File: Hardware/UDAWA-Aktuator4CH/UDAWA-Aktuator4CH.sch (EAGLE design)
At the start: 20 parts

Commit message: PCB Print Ready
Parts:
- added RELAY_PWR: (no value), con-wago-500:W237-102
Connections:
- net 5V: now also RELAY_PWR-2.KL
- net GND: now also RELAY_PWR-1.KL
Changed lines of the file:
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@@
 </class>
 </classes>
-<groups>
-<schematic_group name="RELAY_CONTROL"/>
-</groups>
 <parts>
 <part name="U$1" library="ESP32-DEVKITV1" deviceset="ESP32DEVKITV1" device=""/>
@@
 <part name="CH4" library="con-wago-500" deviceset="W237-102" device="" package3d_urn="urn:adsk.eagle:package:10688/1"/>
 <part name="MAIN_IN" library="con-wago-500" deviceset="W237-102" device="" package3d_urn="urn:adsk.eagle:package:10688/1"/>
+<part name="RELAY_PWR" library="con-wago-500" deviceset="W237-102" device="" package3d_urn="urn:adsk.eagle:package:10688/1"/>
 </parts>
 <sheets>
@@
 <attribute name="NAME" x="-43.18" y="21.209" size="1.778" layer="95" rot="R180"/>
 </instance>
-<instance part="RELAY1" gate="-1" x="86.36" y="-15.24" smashed="yes" grouprefs="RELAY_CONTROL">
+<instance part="RELAY1" gate="-1" x="86.36" y="-15.24" smashed="yes">
 <attribute name="NAME" x="86.36" y="-14.351" size="1.778" layer="95" rot="R180"/>
 </instance>
-<instance part="RELAY1" gate="-2" x="86.36" y="-20.32" smashed="yes" grouprefs="RELAY_CONTROL">
+<instance part="RELAY1" gate="-2" x="86.36" y="-20.32" smashed="yes">
 <attribute name="VALUE" x="83.82" y="-24.003" size="1.778" layer="96"/>
 <attribute name="NAME" x="86.36" y="-19.431" size="1.778" layer="95" rot="R180"/>
 </instance>
-<instance part="RELAY2" gate="-1" x="86.36" y="-5.08" smashed="yes" grouprefs="RELAY_CONTROL">
+<instance part="RELAY2" gate="-1" x="86.36" y="-5.08" smashed="yes">
 <attribute name="NAME" x="86.36" y="-4.191" size="1.778" layer="95" rot="R180"/>
 </instance>
-<instance part="RELAY2" gate="-2" x="86.36" y="-10.16" smashed="yes" grouprefs="RELAY_CONTROL">
+<instance part="RELAY2" gate="-2" x="86.36" y="-10.16" smashed="yes">
 <attribute name="VALUE" x="83.82" y="-13.843" size="1.778" layer="96"/>
 <attribute name="NAME" x="86.36" y="-9.271" size="1.778" layer="95" rot="R180"/>
@@
 <attribute name="VALUE" x="-13.97" y="-66.421" size="1.778" layer="96"/>
 </instance>
-<instance part="RELAY3" gate="-1" x="86.36" y="5.08" smashed="yes" grouprefs="RELAY_CONTROL">
+<instance part="RELAY3" gate="-1" x="86.36" y="5.08" smashed="yes">
 <attribute name="NAME" x="86.36" y="5.969" size="1.778" layer="95" rot="R180"/>
 </instance>
-<instance part="RELAY3" gate="-2" x="86.36" y="0" smashed="yes" grouprefs="RELAY_CONTROL">
+<instance part="RELAY3" gate="-2" x="86.36" y="0" smashed="yes">
 <attribute name="VALUE" x="83.82" y="-3.683" size="1.778" layer="96"/>
 <attribute name="NAME" x="86.36" y="0.889" size="1.778" layer="95" rot="R180"/>
 </instance>
-<instance part="RELAY4" gate="-1" x="86.36" y="15.24" smashed="yes" grouprefs="RELAY_CONTROL">
+<instance part="RELAY4" gate="-1" x="86.36" y="15.24" smashed="yes">
 <attribute name="NAME" x="86.36" y="16.129" size="1.778" layer="95" rot="R180"/>
 </instance>
-<instance part="RELAY4" gate="-2" x="86.36" y="10.16" smashed="yes" grouprefs="RELAY_CONTROL">
+<instance part="RELAY4" gate="-2" x="86.36" y="10.16" smashed="yes">
 <attribute name="VALUE" x="83.82" y="6.477" size="1.778" layer="96"/>
 <attribute name="NAME" x="86.36" y="11.049" size="1.778" layer="95" rot="R180"/>
@@
 <attribute name="VALUE" x="-55.88" y="-24.003" size="1.778" layer="96"/>
 <attribute name="NAME" x="-53.34" y="-19.431" size="1.778" layer="95" rot="R180"/>
+</instance>
+<instance part="RELAY_PWR" gate="-1" x="86.36" y="-27.94" smashed="yes">
+<attribute name="NAME" x="86.36" y="-27.051" size="1.778" layer="95" rot="R180"/>
+</instance>
+<instance part="RELAY_PWR" gate="-2" x="86.36" y="-33.02" smashed="yes">
+<attribute name="VALUE" x="83.82" y="-36.703" size="1.778" layer="96"/>
+<attribute name="NAME" x="86.36" y="-32.131" size="1.778" layer="95" rot="R180"/>
 </instance>
 </instances>
@@
 <segment>
 <pinref part="RELAY1" gate="-1" pin="KL"/>
-<wire x1="91.44" y1="-15.24" x2="93.98" y2="-15.24" width="0.1524" layer="91" grouprefs="RELAY_CONTROL"/>
-<label x="93.98" y="-15.24" size="1.27" layer="95" xref="yes" grouprefs="RELAY_CONTROL"/>
+<wire x1="91.44" y1="-15.24" x2="93.98" y2="-15.24" width="0.1524" layer="91"/>
+<label x="93.98" y="-15.24" size="1.27" layer="95" xref="yes"/>
 </segment>
 <segment>
 <pinref part="RELAY2" gate="-1" pin="KL"/>
-<wire x1="91.44" y1="-5.08" x2="93.98" y2="-5.08" width="0.1524" layer="91" grouprefs="RELAY_CONTROL"/>
-<label x="93.98" y="-5.08" size="1.27" layer="95" xref="yes" grouprefs="RELAY_CONTROL"/>
+<wire x1="91.44" y1="-5.08" x2="93.98" y2="-5.08" width="0.1524" layer="91"/>
+<label x="93.98" y="-5.08" size="1.27" layer="95" xref="yes"/>
 </segment>
 <segment>
 <pinref part="RELAY3" gate="-1" pin="KL"/>
-<wire x1="91.44" y1="5.08" x2="93.98" y2="5.08" width="0.1524" layer="91" grouprefs="RELAY_CONTROL"/>
-<label x="93.98" y="5.08" size="1.27" layer="95" xref="yes" grouprefs="RELAY_CONTROL"/>
+<wire x1="91.44" y1="5.08" x2="93.98" y2="5.08" width="0.1524" layer="91"/>
+<label x="93.98" y="5.08" size="1.27" layer="95" xref="yes"/>
 </segment>
 <segment>
 <pinref part="RELAY4" gate="-1" pin="KL"/>
-<wire x1="91.44" y1="15.24" x2="93.98" y2="15.24" width="0.1524" layer="91" grouprefs="RELAY_CONTROL"/>
-<label x="93.98" y="15.24" size="1.27" layer="95" xref="yes" grouprefs="RELAY_CONTROL"/>
+<wire x1="91.44" y1="15.24" x2="93.98" y2="15.24" width="0.1524" layer="91"/>
+<label x="93.98" y="15.24" size="1.27" layer="95" xref="yes"/>
+</segment>
+<segment>
+<pinref part="RELAY_PWR" gate="-1" pin="KL"/>
+<wire x1="91.44" y1="-27.94" x2="93.98" y2="-27.94" width="0.1524" layer="91"/>
+<label x="93.98" y="-27.94" size="1.778" layer="95" xref="yes"/>
 </segment>
 </net>
@@
 <label x="22.86" y="17.78" size="1.524" layer="95" rot="R90" xref="yes"/>
 </segment>
+<segment>
+<pinref part="RELAY_PWR" gate="-2" pin="KL"/>
+<wire x1="91.44" y1="-33.02" x2="93.98" y2="-33.02" width="0.1524" layer="91"/>
+<label x="93.98" y="-33.02" size="1.778" layer="95" xref="yes"/>
+</segment>
 </net>
 <net name="AC1" class="0">
@@
 <segment>
 <pinref part="RELAY4" gate="-2" pin="KL"/>
-<wire x1="91.44" y1="10.16" x2="93.98" y2="10.16" width="0.1524" layer="91" grouprefs="RELAY_CONTROL"/>
-<label x="93.98" y="10.16" size="1.27" layer="95" xref="yes" grouprefs="RELAY_CONTROL"/>
+<wire x1="91.44" y1="10.16" x2="93.98" y2="10.16" width="0.1524" layer="91"/>
+<label x="93.98" y="10.16" size="1.27" layer="95" xref="yes"/>
 </segment>
 </net>
@@
 <segment>
 <pinref part="RELAY3" gate="-2" pin="KL"/>
-<wire x1="91.44" y1="0" x2="93.98" y2="0" width="0.1524" layer="91" grouprefs="RELAY_CONTROL"/>
-<label x="93.98" y="0" size="1.27" layer="95" xref="yes" grouprefs="RELAY_CONTROL"/>
+<wire x1="91.44" y1="0" x2="93.98" y2="0" width="0.1524" layer="91"/>
+<label x="93.98" y="0" size="1.27" layer="95" xref="yes"/>
 </segment>
 </net>
@@
 <segment>
 <pinref part="RELAY2" gate="-2" pin="KL"/>
-<wire x1="91.44" y1="-10.16" x2="93.98" y2="-10.16" width="0.1524" layer="91" grouprefs="RELAY_CONTROL"/>
-<label x="93.98" y="-10.16" size="1.27" layer="95" xref="yes" grouprefs="RELAY_CONTROL"/>
+<wire x1="91.44" y1="-10.16" x2="93.98" y2="-10.16" width="0.1524" layer="91"/>
+<label x="93.98" y="-10.16" size="1.27" layer="95" xref="yes"/>
 </segment>
 </net>
@@
 <segment>
 <pinref part="RELAY1" gate="-2" pin="KL"/>
-<wire x1="91.44" y1="-20.32" x2="93.98" y2="-20.32" width="0.1524" layer="91" grouprefs="RELAY_CONTROL"/>
-<label x="93.98" y="-20.32" size="1.27" layer="95" xref="yes" grouprefs="RELAY_CONTROL"/>
+<wire x1="91.44" y1="-20.32" x2="93.98" y2="-20.32" width="0.1524" layer="91"/>
+<label x="93.98" y="-20.32" size="1.27" layer="95" xref="yes"/>
 </segment>
 </net>
@@
 packages will not be understood (or retained) with this version.
 </note>
-<note version="9.5" severity="warning">
-Since Version 9.5, EAGLE supports persistent groups with
-schematics, and board files. Those persistent groups
-will not be understood (or retained) with this version.
-</note>
 </compatibility>

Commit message: Revisi terminal catu daya. Solar panel support.
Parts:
- added MCU_PWR_IN, PSU_5V: (no value), con-wago-500:W237-102
- renumbered MAIN_IN to LOAD_IN
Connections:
- net VCC renamed 3V3
- removed net GND2: U$1.GND@2
- new net VIN: MCU_PWR_IN-2.KL, U$1.VIN
- net 5V: now also PSU_5V-2.KL; no longer U$1.VIN
- net GND: now also MCU_PWR_IN-1.KL, PSU_5V-1.KL, U$1.GND@2

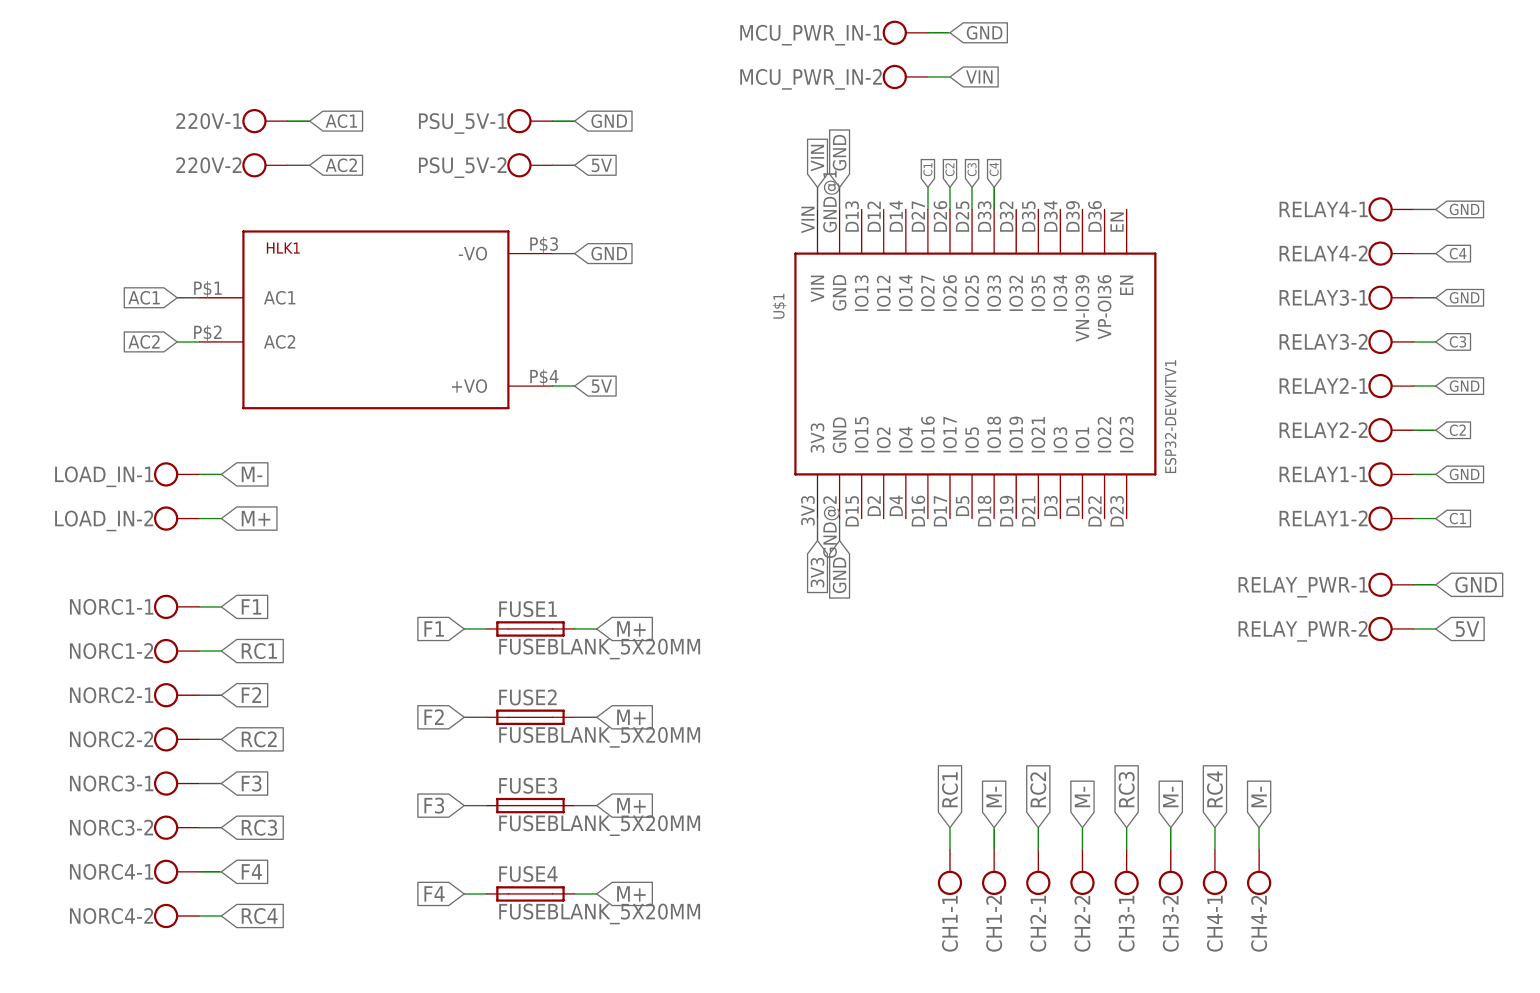
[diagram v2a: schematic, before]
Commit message: revisi fuse holder ke SH22,5A (Version 1)
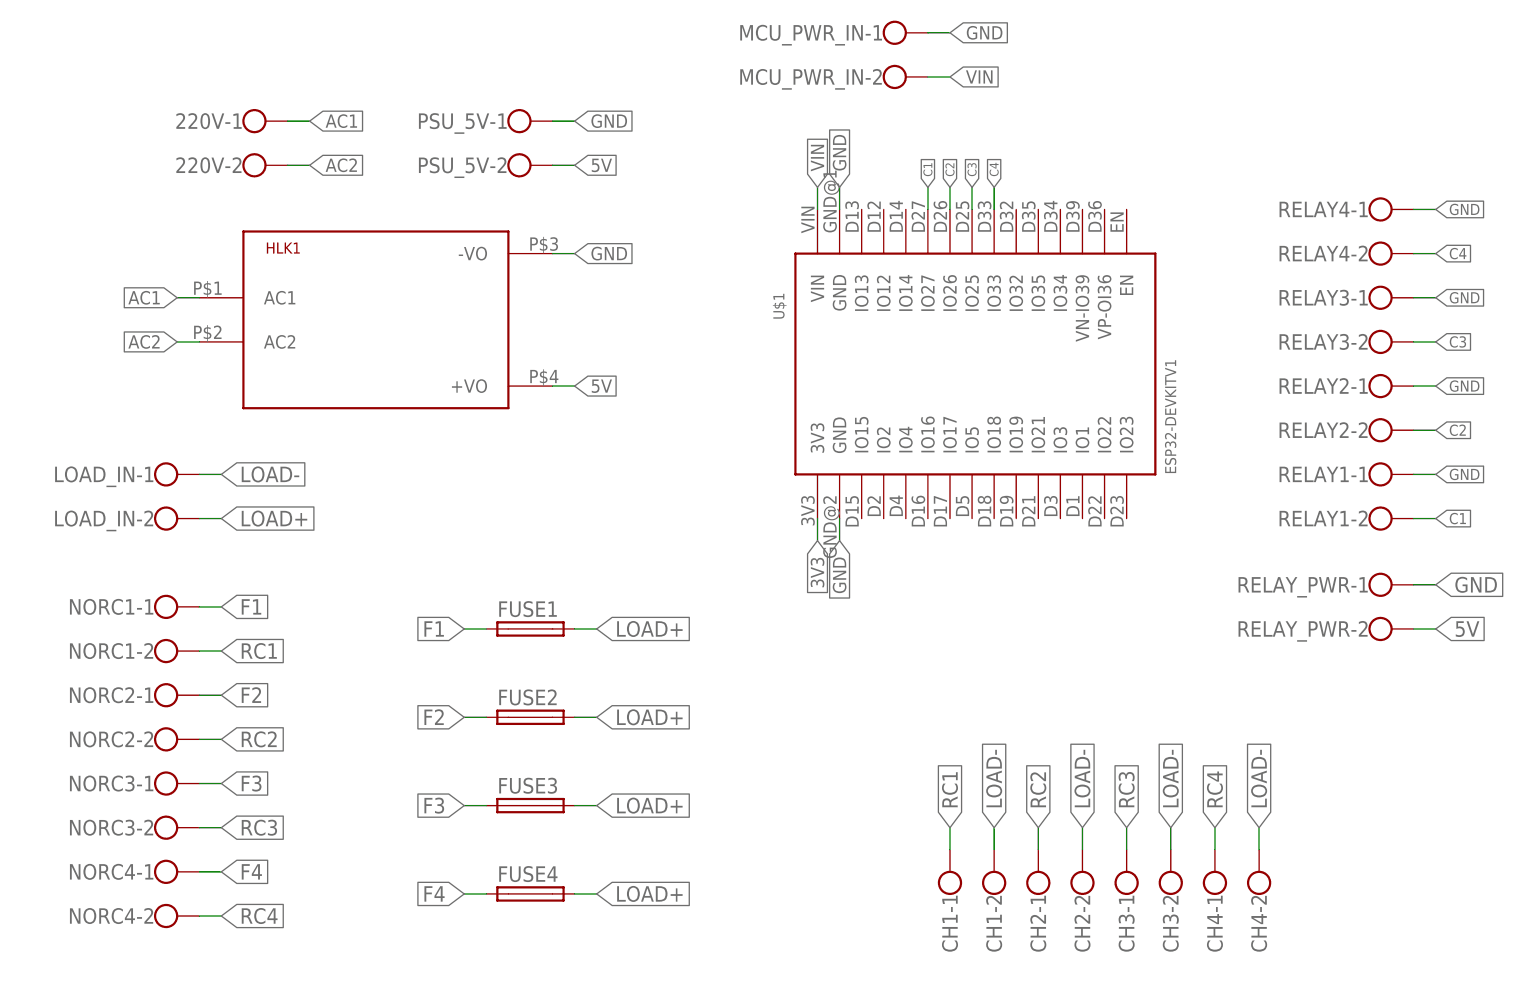
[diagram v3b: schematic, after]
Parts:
- FUSE1, FUSE2, FUSE3, FUSE4: value FUSEBLANK_5X20MM -> (none); device fuse:FUSEBLANK_5X20MM -> fuse:SH22,5A
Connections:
- net M+ renamed LOAD+
- net M- renamed LOAD-
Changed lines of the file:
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@@
 <part name="RELAY1" library="con-wago-500" deviceset="W237-102" device="" package3d_urn="urn:adsk.eagle:package:10688/1"/>
 <part name="RELAY2" library="con-wago-500" deviceset="W237-102" device="" package3d_urn="urn:adsk.eagle:package:10688/1"/>
-<part name="FUSE1" library="fuse" deviceset="FUSE" device="BLANK_5X20MM" package3d_urn="urn:adsk.eagle:package:14079/1"/>
-<part name="FUSE2" library="fuse" deviceset="FUSE" device="BLANK_5X20MM" package3d_urn="urn:adsk.eagle:package:14079/1"/>
-<part name="FUSE3" library="fuse" deviceset="FUSE" device="BLANK_5X20MM" package3d_urn="urn:adsk.eagle:package:14079/1"/>
-<part name="FUSE4" library="fuse" deviceset="FUSE" device="BLANK_5X20MM" package3d_urn="urn:adsk.eagle:package:14079/1"/>
+<part name="FUSE1" library="fuse" deviceset="SH22,5A" device="" package3d_urn="urn:adsk.eagle:package:14070/1"/>
+<part name="FUSE2" library="fuse" deviceset="SH22,5A" device="" package3d_urn="urn:adsk.eagle:package:14070/1"/>
+<part name="FUSE3" library="fuse" deviceset="SH22,5A" device="" package3d_urn="urn:adsk.eagle:package:14070/1"/>
+<part name="FUSE4" library="fuse" deviceset="SH22,5A" device="" package3d_urn="urn:adsk.eagle:package:14070/1"/>
 <part name="RELAY3" library="con-wago-500" deviceset="W237-102" device="" package3d_urn="urn:adsk.eagle:package:10688/1"/>
 <part name="RELAY4" library="con-wago-500" deviceset="W237-102" device="" package3d_urn="urn:adsk.eagle:package:10688/1"/>
@@
 <attribute name="NAME" x="86.36" y="-9.271" size="1.778" layer="95" rot="R180"/>
 </instance>
-<instance part="FUSE1" gate="G$1" x="-10.16" y="-33.02" smashed="yes">
+<instance part="FUSE1" gate="1" x="-10.16" y="-33.02" smashed="yes">
 <attribute name="NAME" x="-13.97" y="-31.623" size="1.778" layer="95"/>
 <attribute name="VALUE" x="-13.97" y="-35.941" size="1.778" layer="96"/>
 </instance>
-<instance part="FUSE2" gate="G$1" x="-10.16" y="-43.18" smashed="yes">
+<instance part="FUSE2" gate="1" x="-10.16" y="-43.18" smashed="yes">
 <attribute name="NAME" x="-13.97" y="-41.783" size="1.778" layer="95"/>
 <attribute name="VALUE" x="-13.97" y="-46.101" size="1.778" layer="96"/>
 </instance>
-<instance part="FUSE3" gate="G$1" x="-10.16" y="-53.34" smashed="yes">
+<instance part="FUSE3" gate="1" x="-10.16" y="-53.34" smashed="yes">
 <attribute name="NAME" x="-13.97" y="-51.943" size="1.778" layer="95"/>
 <attribute name="VALUE" x="-13.97" y="-56.261" size="1.778" layer="96"/>
 </instance>
-<instance part="FUSE4" gate="G$1" x="-10.16" y="-63.5" smashed="yes">
+<instance part="FUSE4" gate="1" x="-10.16" y="-63.5" smashed="yes">
 <attribute name="NAME" x="-13.97" y="-62.103" size="1.778" layer="95"/>
 <attribute name="VALUE" x="-13.97" y="-66.421" size="1.778" layer="96"/>
@@
 </segment>
 </net>
-<net name="M-" class="0">
+<net name="LOAD-" class="0">
 <segment>
 <pinref part="LOAD_IN" gate="-1" pin="KL"/>
@@
 </segment>
 </net>
-<net name="M+" class="0">
+<net name="LOAD+" class="0">
 <segment>
 <pinref part="LOAD_IN" gate="-2" pin="KL"/>
@@
 </segment>
 <segment>
-<pinref part="FUSE1" gate="G$1" pin="2"/>
+<pinref part="FUSE1" gate="1" pin="2"/>
 <wire x1="-5.08" y1="-33.02" x2="-2.54" y2="-33.02" width="0.1524" layer="91"/>
 <label x="-2.54" y="-33.02" size="1.778" layer="95" xref="yes"/>
 </segment>
 <segment>
-<pinref part="FUSE2" gate="G$1" pin="2"/>
+<pinref part="FUSE2" gate="1" pin="2"/>
 <wire x1="-5.08" y1="-43.18" x2="-2.54" y2="-43.18" width="0.1524" layer="91"/>
 <label x="-2.54" y="-43.18" size="1.778" layer="95" xref="yes"/>
 </segment>
 <segment>
-<pinref part="FUSE3" gate="G$1" pin="2"/>
+<pinref part="FUSE3" gate="1" pin="2"/>
 <wire x1="-5.08" y1="-53.34" x2="-2.54" y2="-53.34" width="0.1524" layer="91"/>
 <label x="-2.54" y="-53.34" size="1.778" layer="95" xref="yes"/>
 </segment>
 <segment>
-<pinref part="FUSE4" gate="G$1" pin="2"/>
+<pinref part="FUSE4" gate="1" pin="2"/>
 <wire x1="-5.08" y1="-63.5" x2="-2.54" y2="-63.5" width="0.1524" layer="91"/>
 <label x="-2.54" y="-63.5" size="1.778" layer="95" xref="yes"/>
@@
 <net name="F1" class="0">
 <segment>
-<pinref part="FUSE1" gate="G$1" pin="1"/>
+<pinref part="FUSE1" gate="1" pin="1"/>
 <wire x1="-15.24" y1="-33.02" x2="-17.78" y2="-33.02" width="0.1524" layer="91"/>
 <label x="-17.78" y="-33.02" size="1.778" layer="95" rot="R180" xref="yes"/>
@@
 </segment>
 <segment>
-<pinref part="FUSE2" gate="G$1" pin="1"/>
+<pinref part="FUSE2" gate="1" pin="1"/>
 <wire x1="-15.24" y1="-43.18" x2="-17.78" y2="-43.18" width="0.1524" layer="91"/>
 <label x="-17.78" y="-43.18" size="1.778" layer="95" rot="R180" xref="yes"/>
@@
 </segment>
 <segment>
-<pinref part="FUSE3" gate="G$1" pin="1"/>
+<pinref part="FUSE3" gate="1" pin="1"/>
 <wire x1="-15.24" y1="-53.34" x2="-17.78" y2="-53.34" width="0.1524" layer="91"/>
 <label x="-17.78" y="-53.34" size="1.778" layer="95" rot="R180" xref="yes"/>
@@
 </segment>
 <segment>
-<pinref part="FUSE4" gate="G$1" pin="1"/>
+<pinref part="FUSE4" gate="1" pin="1"/>
 <wire x1="-15.24" y1="-63.5" x2="-17.78" y2="-63.5" width="0.1524" layer="91"/>
 <label x="-17.78" y="-63.5" size="1.778" layer="95" rot="R180" xref="yes"/>
